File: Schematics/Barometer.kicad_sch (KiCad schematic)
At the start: 4 parts

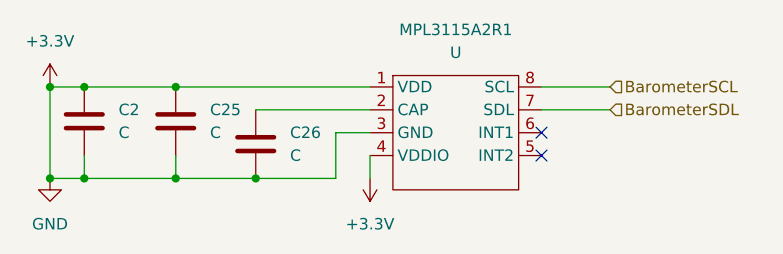
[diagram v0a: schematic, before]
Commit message: added LCSC numbers and footprint values, need to connect schemeatic pins, then can start layout
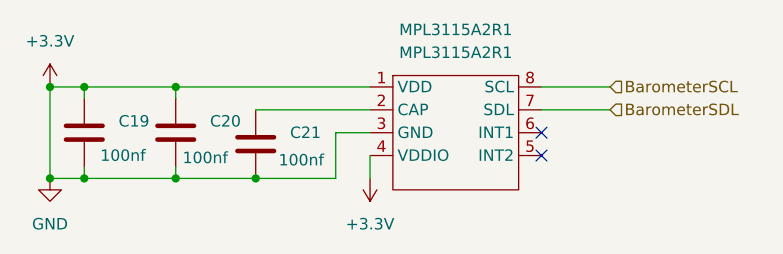
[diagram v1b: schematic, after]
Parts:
- C19: renamed from C2; value C -> 100nf; footprint (none) -> Capacitor_SMD:C_0805_2012Metric_Pad1.18x1.45mm_HandSolder; LCSC Part (none) -> C49678
- C20: renamed from C25; value C -> 100nf; footprint (none) -> Capacitor_SMD:C_0805_2012Metric_Pad1.18x1.45mm_HandSolder; LCSC Part (none) -> C49678
- C21: renamed from C26; value C -> 100nf; footprint (none) -> Capacitor_SMD:C_0805_2012Metric_Pad1.18x1.45mm_HandSolder; LCSC Part (none) -> C49678
- MPL3115A2R1: value U -> MPL3115A2R1; footprint (none) -> myFootprints:PSON80P300X300X100-8N; LCSC Part (none) -> C54429
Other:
- moved on the sheet: C19, C20
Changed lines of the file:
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@@
+	(wire
+		(pts
+			(xy 110.49 77.47) (xy 110.49 76.2)
+		)
+		(stroke
+			(width 0)
+			(type default)
+		)
+	)
 	(wire
 		(pts
@@
 	(wire
 		(pts
-			(xy 110.49 83.82) (xy 110.49 86.36)
+			(xy 110.49 85.09) (xy 110.49 86.36)
 		)
 		(stroke
@@
 	(wire
 		(pts
+			(xy 100.33 77.47) (xy 100.33 76.2)
+		)
+		(stroke
+			(width 0)
+			(type default)
+		)
+	)
+	(wire
+		(pts
 			(xy 119.38 86.36) (xy 110.49 86.36)
 		)
@@
 	(wire
 		(pts
-			(xy 100.33 83.82) (xy 100.33 86.36)
+			(xy 100.33 85.09) (xy 100.33 86.36)
 		)
 		(stroke
@@
 		(dnp no)
 		(fields_autoplaced yes)
-		(property "Reference" "#PWR071"
+		(property "Reference" "#PWR065"
 			(at 96.52 92.71 0)
 			(effects
@@
 			(project ""
 				(path "/6cb3dda3-5fe8-4715-b831-354360aa3199/4fd02220-789e-446c-b98b-396c4e06173f"
-					(reference "#PWR071")
+					(reference "#PWR065")
 					(unit 1)
 				)
@@
 	(symbol
 		(lib_id "Device:C")
-		(at 100.33 80.01 0)
+		(at 100.33 81.28 0)
 		(unit 1)
 		(exclude_from_sim no)
@@
 		(on_board yes)
 		(dnp no)
-		(fields_autoplaced yes)
-		(property "Reference" "C2"
-			(at 104.14 78.7399 0)
+		(property "Reference" "C19"
+			(at 104.14 80.0099 0)
 			(effects
 				(font
@@
 			)
 		)
-		(property "Value" "C"
-			(at 104.14 81.2799 0)
+		(property "Value" "100nf"
+			(at 102.108 83.82 0)
 			(effects
 				(font
@@
 			)
 		)
-		(property "Footprint" ""
-			(at 101.2952 83.82 0)
+		(property "Footprint" "Capacitor_SMD:C_0805_2012Metric_Pad1.18x1.45mm_HandSolder"
+			(at 101.2952 85.09 0)
 			(effects
 				(font
@@
 		)
 		(property "Datasheet" "~"
-			(at 100.33 80.01 0)
+			(at 100.33 81.28 0)
 			(effects
 				(font
@@
 		)
 		(property "Description" "Unpolarized capacitor"
-			(at 100.33 80.01 0)
+			(at 100.33 81.28 0)
+			(effects
+				(font
+					(size 1.27 1.27)
+				)
+				(hide yes)
+			)
+		)
+		(property "Sim.Device" ""
+			(at 100.33 81.28 0)
+			(effects
+				(font
+					(size 1.27 1.27)
+				)
+				(hide yes)
+			)
+		)
+		(property "Sim.Type" ""
+			(at 100.33 81.28 0)
+			(effects
+				(font
+					(size 1.27 1.27)
+				)
+				(hide yes)
+			)
+		)
+		(property "LCSC Part" "C49678"
+			(at 100.33 81.28 0)
 			(effects
 				(font
@@
 			(project ""
 				(path "/6cb3dda3-5fe8-4715-b831-354360aa3199/4fd02220-789e-446c-b98b-396c4e06173f"
-					(reference "C2")
+					(reference "C19")
 					(unit 1)
 				)
@@
 		(dnp no)
 		(fields_autoplaced yes)
-		(property "Reference" "#PWR072"
+		(property "Reference" "#PWR064"
 			(at 96.52 80.01 0)
 			(effects
@@
 			(project ""
 				(path "/6cb3dda3-5fe8-4715-b831-354360aa3199/4fd02220-789e-446c-b98b-396c4e06173f"
-					(reference "#PWR072")
+					(reference "#PWR064")
 					(unit 1)
 				)
@@
 			)
 		)
-		(property "Value" "U"
+		(property "Value" "MPL3115A2R1"
 			(at 141.605 72.39 0)
 			(effects
@@
 			)
 		)
-		(property "Footprint" ""
+		(property "Footprint" "myFootprints:PSON80P300X300X100-8N"
 			(at 137.16 82.55 0)
 			(effects
@@
 		)
 		(property "Description" ""
+			(at 137.16 82.55 0)
+			(effects
+				(font
+					(size 1.27 1.27)
+				)
+				(hide yes)
+			)
+		)
+		(property "Sim.Device" ""
+			(at 137.16 82.55 0)
+			(effects
+				(font
+					(size 1.27 1.27)
+				)
+				(hide yes)
+			)
+		)
+		(property "Sim.Type" ""
+			(at 137.16 82.55 0)
+			(effects
+				(font
+					(size 1.27 1.27)
+				)
+				(hide yes)
+			)
+		)
+		(property "LCSC Part" "C54429"
 			(at 137.16 82.55 0)
 			(effects
@@
 	(symbol
 		(lib_id "Device:C")
-		(at 110.49 80.01 0)
+		(at 110.49 81.28 0)
 		(unit 1)
 		(exclude_from_sim no)
@@
 		(on_board yes)
 		(dnp no)
-		(fields_autoplaced yes)
-		(property "Reference" "C25"
-			(at 114.3 78.7399 0)
+		(property "Reference" "C20"
+			(at 114.3 80.0099 0)
 			(effects
 				(font
@@
 			)
 		)
-		(property "Value" "C"
-			(at 114.3 81.2799 0)
+		(property "Value" "100nf"
+			(at 111.252 84.074 0)
 			(effects
 				(font
@@
 			)
 		)
-		(property "Footprint" ""
-			(at 111.4552 83.82 0)
+		(property "Footprint" "Capacitor_SMD:C_0805_2012Metric_Pad1.18x1.45mm_HandSolder"
+			(at 111.4552 85.09 0)
 			(effects
 				(font
@@
 		)
 		(property "Datasheet" "~"
-			(at 110.49 80.01 0)
+			(at 110.49 81.28 0)
 			(effects
 				(font
@@
 		)
 		(property "Description" "Unpolarized capacitor"
-			(at 110.49 80.01 0)
+			(at 110.49 81.28 0)
+			(effects
+				(font
+					(size 1.27 1.27)
+				)
+				(hide yes)
+			)
+		)
+		(property "Sim.Device" ""
+			(at 110.49 81.28 0)
+			(effects
+				(font
+					(size 1.27 1.27)
+				)
+				(hide yes)
+			)
+		)
+		(property "Sim.Type" ""
+			(at 110.49 81.28 0)
+			(effects
+				(font
+					(size 1.27 1.27)
+				)
+				(hide yes)
+			)
+		)
+		(property "LCSC Part" "C49678"
+			(at 110.49 81.28 0)
 			(effects
 				(font
@@
 			(project "flightcomputer2"
 				(path "/6cb3dda3-5fe8-4715-b831-354360aa3199/4fd02220-789e-446c-b98b-396c4e06173f"
-					(reference "C25")
+					(reference "C20")
 					(unit 1)
 				)
@@
 		(dnp no)
 		(fields_autoplaced yes)
-		(property "Reference" "#PWR073"
+		(property "Reference" "#PWR066"
 			(at 132.08 82.55 0)
 			(effects
@@
 			(project ""
 				(path "/6cb3dda3-5fe8-4715-b831-354360aa3199/4fd02220-789e-446c-b98b-396c4e06173f"
-					(reference "#PWR073")
+					(reference "#PWR066")
 					(unit 1)
 				)
@@
 		(on_board yes)
 		(dnp no)
-		(fields_autoplaced yes)
-		(property "Reference" "C26"
+		(property "Reference" "C21"
 			(at 123.19 81.2799 0)
 			(effects
@@
 			)
 		)
-		(property "Value" "C"
-			(at 123.19 83.8199 0)
+		(property "Value" "100nf"
+			(at 121.92 84.328 0)
 			(effects
 				(font
@@
 			)
 		)
-		(property "Footprint" ""
+		(property "Footprint" "Capacitor_SMD:C_0805_2012Metric_Pad1.18x1.45mm_HandSolder"
 			(at 120.3452 86.36 0)
 			(effects
@@
 		)
 		(property "Description" "Unpolarized capacitor"
+			(at 119.38 82.55 0)
+			(effects
+				(font
+					(size 1.27 1.27)
+				)
+				(hide yes)
+			)
+		)
+		(property "Sim.Device" ""
+			(at 119.38 82.55 0)
+			(effects
+				(font
+					(size 1.27 1.27)
+				)
+				(hide yes)
+			)
+		)
+		(property "Sim.Type" ""
+			(at 119.38 82.55 0)
+			(effects
+				(font
+					(size 1.27 1.27)
+				)
+				(hide yes)
+			)
+		)
+		(property "LCSC Part" "C49678"
 			(at 119.38 82.55 0)
 			(effects
@@
 			(project "flightcomputer2"
 				(path "/6cb3dda3-5fe8-4715-b831-354360aa3199/4fd02220-789e-446c-b98b-396c4e06173f"
-					(reference "C26")
+					(reference "C21")
 					(unit 1)
 				)

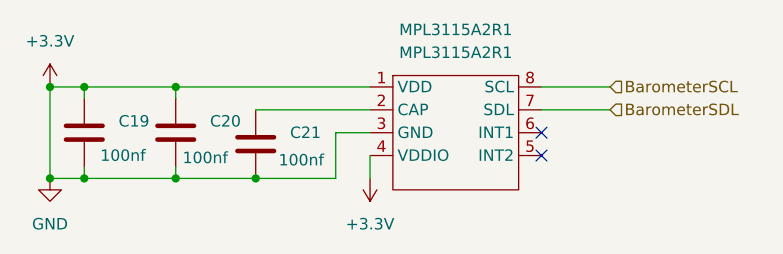
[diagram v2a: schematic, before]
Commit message: fixed symbols and added diodes to power input before ldo
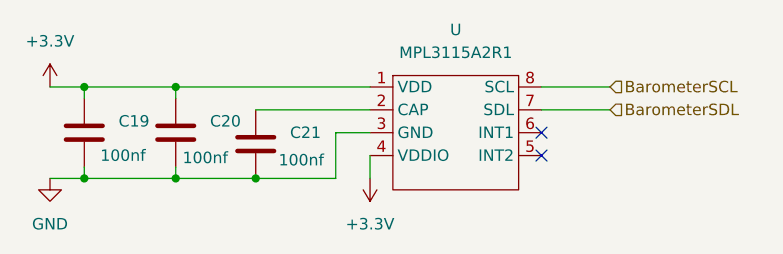
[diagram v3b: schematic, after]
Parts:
- renumbered MPL3115A2R1 to U
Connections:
- net +3.3V: no longer C19.2, C20.2, C21.2, U.3 (GND)
- new net GND: C19.2, C20.2, C21.2, U.3 (GND)
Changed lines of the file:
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@@
 	(paper "A4")
-	(junction
-		(at 96.52 86.36)
-		(diameter 0)
-		(color 0 0 0 0)
-	)
 	(junction
 		(at 100.33 76.2)
@@
 	)
 	(junction
-		(at 96.52 76.2)
-		(diameter 0)
-		(color 0 0 0 0)
-	)
-	(junction
 		(at 119.38 86.36)
 		(diameter 0)
@@
 		(pts
 			(xy 119.38 86.36) (xy 110.49 86.36)
-		)
-		(stroke
-			(width 0)
-			(type default)
-		)
-	)
-	(wire
-		(pts
-			(xy 96.52 86.36) (xy 96.52 76.2)
 		)
 		(stroke
@@
 		(dnp no)
 		(fields_autoplaced yes)
-		(property "Reference" "MPL3115A2R1"
+		(property "Reference" "U"
 			(at 141.605 69.85 0)
 			(effects
@@
 			(project ""
 				(path "/6cb3dda3-5fe8-4715-b831-354360aa3199/4fd02220-789e-446c-b98b-396c4e06173f"
-					(reference "MPL3115A2R1")
+					(reference "U")
 					(unit 1)
 				)

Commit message: added lora correct and organizing sheet pins
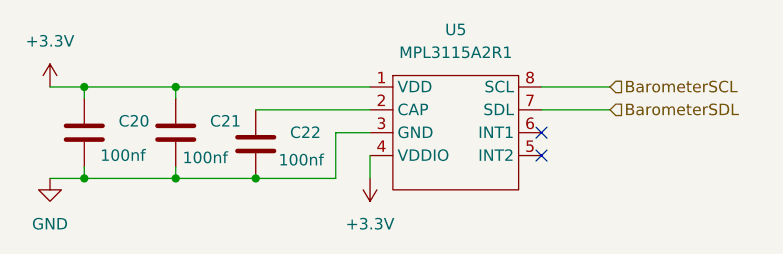
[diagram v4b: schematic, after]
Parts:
- U5: renamed from U; footprint myFootprints:PSON80P300X300X100-8N -> Package_LGA:LGA-8_3x5mm_P1.25mm; LCSC Part C54429 -> (none)
- renumbered C19 to C20, C20 to C21, C21 to C22
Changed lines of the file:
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@@
 		(dnp no)
 		(fields_autoplaced yes)
-		(property "Reference" "#PWR065"
+		(property "Reference" "#PWR068"
 			(at 96.52 92.71 0)
 			(effects
@@
 			(project ""
 				(path "/6cb3dda3-5fe8-4715-b831-354360aa3199/4fd02220-789e-446c-b98b-396c4e06173f"
-					(reference "#PWR065")
+					(reference "#PWR068")
 					(unit 1)
 				)
@@
 		(on_board yes)
 		(dnp no)
-		(property "Reference" "C19"
+		(property "Reference" "C20"
 			(at 104.14 80.0099 0)
 			(effects
@@
 			(project ""
 				(path "/6cb3dda3-5fe8-4715-b831-354360aa3199/4fd02220-789e-446c-b98b-396c4e06173f"
-					(reference "C19")
+					(reference "C20")
 					(unit 1)
 				)
@@
 		(dnp no)
 		(fields_autoplaced yes)
-		(property "Reference" "#PWR064"
+		(property "Reference" "#PWR067"
 			(at 96.52 80.01 0)
 			(effects
@@
 			(project ""
 				(path "/6cb3dda3-5fe8-4715-b831-354360aa3199/4fd02220-789e-446c-b98b-396c4e06173f"
-					(reference "#PWR064")
+					(reference "#PWR067")
 					(unit 1)
 				)
@@
 		(dnp no)
 		(fields_autoplaced yes)
-		(property "Reference" "U"
+		(property "Reference" "U5"
 			(at 141.605 69.85 0)
 			(effects
@@
 			)
 		)
-		(property "Footprint" "myFootprints:PSON80P300X300X100-8N"
+		(property "Footprint" "Package_LGA:LGA-8_3x5mm_P1.25mm"
 			(at 137.16 82.55 0)
 			(effects
@@
 			)
 		)
-		(property "LCSC Part" "C54429"
+		(property "LCSC Part" ""
 			(at 137.16 82.55 0)
 			(effects
@@
 			(project ""
 				(path "/6cb3dda3-5fe8-4715-b831-354360aa3199/4fd02220-789e-446c-b98b-396c4e06173f"
-					(reference "U")
+					(reference "U5")
 					(unit 1)
 				)
@@
 		(on_board yes)
 		(dnp no)
-		(property "Reference" "C20"
+		(property "Reference" "C21"
 			(at 114.3 80.0099 0)
 			(effects
@@
 			(project "flightcomputer2"
 				(path "/6cb3dda3-5fe8-4715-b831-354360aa3199/4fd02220-789e-446c-b98b-396c4e06173f"
-					(reference "C20")
+					(reference "C21")
 					(unit 1)
 				)
@@
 		(dnp no)
 		(fields_autoplaced yes)
-		(property "Reference" "#PWR066"
+		(property "Reference" "#PWR069"
 			(at 132.08 82.55 0)
 			(effects
@@
 			(project ""
 				(path "/6cb3dda3-5fe8-4715-b831-354360aa3199/4fd02220-789e-446c-b98b-396c4e06173f"
-					(reference "#PWR066")
+					(reference "#PWR069")
 					(unit 1)
 				)
@@
 		(on_board yes)
 		(dnp no)
-		(property "Reference" "C21"
+		(property "Reference" "C22"
 			(at 123.19 81.2799 0)
 			(effects
@@
 			(project "flightcomputer2"
 				(path "/6cb3dda3-5fe8-4715-b831-354360aa3199/4fd02220-789e-446c-b98b-396c4e06173f"
-					(reference "C21")
-					(unit 1)
-				)
+					(reference "C22")
+					(unit 1)
+				)

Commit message: finished pin assignments and ran ERC all good ready for layout
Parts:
- U5: LCSC Part (none) -> C54429
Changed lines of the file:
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@@
+			)
+		)
+		(property "Description_1" ""
+			(at 100.33 81.28 0)
+			(effects
+				(font
+					(size 1.27 1.27)
+				)
+				(hide yes)
+			)
+		)
+		(property "MF" ""
+			(at 100.33 81.28 0)
+			(effects
+				(font
+					(size 1.27 1.27)
+				)
+				(hide yes)
+			)
+		)
+		(property "MP" ""
+			(at 100.33 81.28 0)
+			(effects
+				(font
+					(size 1.27 1.27)
+				)
+				(hide yes)
+			)
+		)
+		(property "Package" ""
+			(at 100.33 81.28 0)
+			(effects
+				(font
+					(size 1.27 1.27)
+				)
+				(hide yes)
+			)
+		)
+		(property "Price" ""
+			(at 100.33 81.28 0)
+			(effects
+				(font
+					(size 1.27 1.27)
+				)
+				(hide yes)
+			)
+		)
+		(property "Purchase-URL" ""
+			(at 100.33 81.28 0)
+			(effects
+				(font
+					(size 1.27 1.27)
+				)
+				(hide yes)
 			)
 		)
@@
 			)
 		)
-		(property "LCSC Part" ""
+		(property "LCSC Part" "C54429"
+			(at 137.16 82.55 0)
+			(effects
+				(font
+					(size 1.27 1.27)
+				)
+				(hide yes)
+			)
+		)
+		(property "Description_1" ""
+			(at 137.16 82.55 0)
+			(effects
+				(font
+					(size 1.27 1.27)
+				)
+				(hide yes)
+			)
+		)
+		(property "MF" ""
+			(at 137.16 82.55 0)
+			(effects
+				(font
+					(size 1.27 1.27)
+				)
+				(hide yes)
+			)
+		)
+		(property "MP" ""
+			(at 137.16 82.55 0)
+			(effects
+				(font
+					(size 1.27 1.27)
+				)
+				(hide yes)
+			)
+		)
+		(property "Package" ""
+			(at 137.16 82.55 0)
+			(effects
+				(font
+					(size 1.27 1.27)
+				)
+				(hide yes)
+			)
+		)
+		(property "Price" ""
+			(at 137.16 82.55 0)
+			(effects
+				(font
+					(size 1.27 1.27)
+				)
+				(hide yes)
+			)
+		)
+		(property "Purchase-URL" ""
 			(at 137.16 82.55 0)
 			(effects
@@
 		)
 		(property "LCSC Part" "C49678"
+			(at 110.49 81.28 0)
+			(effects
+				(font
+					(size 1.27 1.27)
+				)
+				(hide yes)
+			)
+		)
+		(property "Description_1" ""
+			(at 110.49 81.28 0)
+			(effects
+				(font
+					(size 1.27 1.27)
+				)
+				(hide yes)
+			)
+		)
+		(property "MF" ""
+			(at 110.49 81.28 0)
+			(effects
+				(font
+					(size 1.27 1.27)
+				)
+				(hide yes)
+			)
+		)
+		(property "MP" ""
+			(at 110.49 81.28 0)
+			(effects
+				(font
+					(size 1.27 1.27)
+				)
+				(hide yes)
+			)
+		)
+		(property "Package" ""
+			(at 110.49 81.28 0)
+			(effects
+				(font
+					(size 1.27 1.27)
+				)
+				(hide yes)
+			)
+		)
+		(property "Price" ""
+			(at 110.49 81.28 0)
+			(effects
+				(font
+					(size 1.27 1.27)
+				)
+				(hide yes)
+			)
+		)
+		(property "Purchase-URL" ""
 			(at 110.49 81.28 0)
 			(effects
@@
 			(at 119.38 82.55 0)
 			(effects
+				(font
+					(size 1.27 1.27)
+				)
+				(hide yes)
+			)
+		)
+		(property "Description_1" ""
+			(at 119.38 82.55 0)
+			(effects
+				(font
+					(size 1.27 1.27)
+				)
+				(hide yes)
+			)
+		)
+		(property "MF" ""
+			(at 119.38 82.55 0)
+			(effects
+				(font
+					(size 1.27 1.27)
+				)
+				(hide yes)
+			)
+		)
+		(property "MP" ""
+			(at 119.38 82.55 0)
+			(effects
+				(font
+					(size 1.27 1.27)
+				)
+				(hide yes)
+			)
+		)
+		(property "Package" ""
+			(at 119.38 82.55 0)
+			(effects
+				(font
+					(size 1.27 1.27)
+				)
+				(hide yes)
+			)
+		)
+		(property "Price" ""
+			(at 119.38 82.55 0)
+			(effects
+				(font
+					(size 1.27 1.27)
+				)
+				(hide yes)
+			)
+		)
+		(property "Purchase-URL" ""
+			(at 119.38 82.55 0)
+			(effects

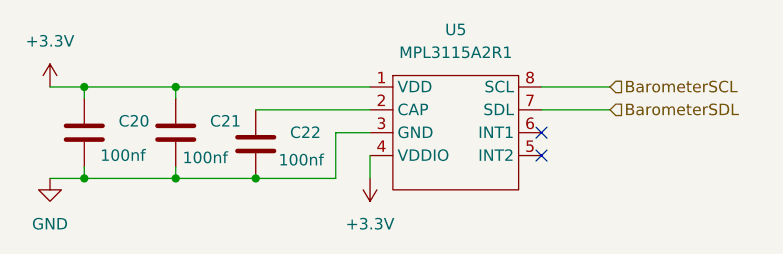
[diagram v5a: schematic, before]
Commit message: first layout need to go over schematic
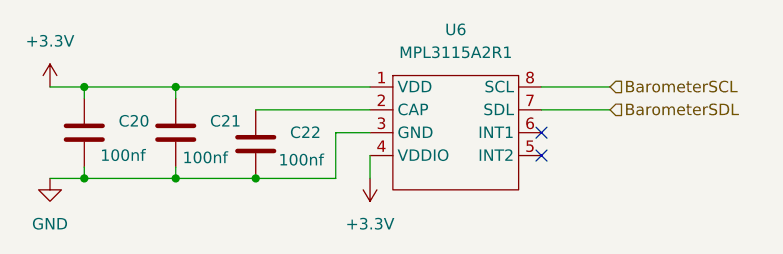
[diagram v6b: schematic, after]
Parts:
- renumbered U5 to U6
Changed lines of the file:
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@@
 		(dnp no)
 		(fields_autoplaced yes)
-		(property "Reference" "#PWR068"
+		(property "Reference" "#PWR074"
 			(at 96.52 92.71 0)
 			(effects
@@
 			(project ""
 				(path "/6cb3dda3-5fe8-4715-b831-354360aa3199/4fd02220-789e-446c-b98b-396c4e06173f"
-					(reference "#PWR068")
+					(reference "#PWR074")
 					(unit 1)
 				)
@@
 		(dnp no)
 		(fields_autoplaced yes)
-		(property "Reference" "#PWR067"
+		(property "Reference" "#PWR073"
 			(at 96.52 80.01 0)
 			(effects
@@
 			(project ""
 				(path "/6cb3dda3-5fe8-4715-b831-354360aa3199/4fd02220-789e-446c-b98b-396c4e06173f"
-					(reference "#PWR067")
+					(reference "#PWR073")
 					(unit 1)
 				)
@@
 		(dnp no)
 		(fields_autoplaced yes)
-		(property "Reference" "U5"
+		(property "Reference" "U6"
 			(at 141.605 69.85 0)
 			(effects
@@
 			(project ""
 				(path "/6cb3dda3-5fe8-4715-b831-354360aa3199/4fd02220-789e-446c-b98b-396c4e06173f"
-					(reference "U5")
+					(reference "U6")
 					(unit 1)
 				)
@@
 		(dnp no)
 		(fields_autoplaced yes)
-		(property "Reference" "#PWR069"
+		(property "Reference" "#PWR075"
 			(at 132.08 82.55 0)
 			(effects
@@
 			(project ""
 				(path "/6cb3dda3-5fe8-4715-b831-354360aa3199/4fd02220-789e-446c-b98b-396c4e06173f"
-					(reference "#PWR069")
+					(reference "#PWR075")
 					(unit 1)
 				)
